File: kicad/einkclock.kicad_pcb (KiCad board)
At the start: 2 copper layers, 80 x 50 mm, 78 parts, among them P1 SWD, Q1 BSH205, Q2 BSH205, Q3 IRLML6244, Q4 IRLML6244, U1 23LC512, U10 DCF77_Generic, U2 LPC1227FBD48/301, U3 TS321ILT, U4 ED060SC4V2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

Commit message: Cleanups
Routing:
- net /E-Ink/-20V: track 101.0 -> 100.2 mm
- net /DCF77/SIG: track 70.0 -> 69.4 mm

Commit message: Cleanups
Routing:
- net /CPU/DON: track 63.5 -> 76.3 mm, vias 3 -> 6
- net Net-(C9-Pad1): track 54.8 -> 66.4 mm
- net GND: track 67.5 -> 74.2 mm, vias 46 -> 45
- net /CPU/DCKV: track 19.9 -> 22.4 mm
- net /CPU/DSPH: track 21.4 -> 19.3 mm
- net /CPU/DOE: track 22.4 -> 20.2 mm
- net /CPU/DCL: track 25.5 -> 23.4 mm
- net /CPU/DSPV: track 13.8 -> 14.6 mm
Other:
- rule trace_min: 0.2 -> 0.25

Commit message: Adjustments
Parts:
- added ?: MountingHole_5mm, Mounting_Holes:MountingHole_5mm, F.Cu at (96.0, 66.0)
- added ?: MountingHole_5mm, Mounting_Holes:MountingHole_5mm, F.Cu at (24.0, 66.0)
- added ?: OSHW-Logo2_7.3x6mm_SilkScreen, Symbols:OSHW-Logo2_7.3x6mm_SilkScreen, F.Cu at (96.0, 23.5)
- moved L3 0.50 mm to (24.0, 39.5)
- moved L6 0.50 mm to (38.5, 39.5)
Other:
- board text added: "+"
- board text added: "-"
- board text added: "E-INK CLOCK REV 1"

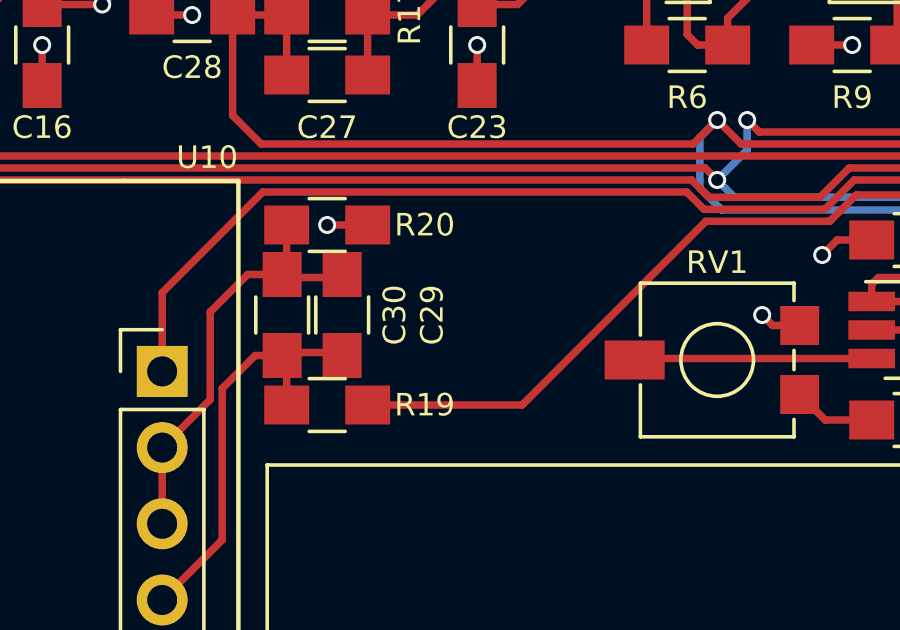
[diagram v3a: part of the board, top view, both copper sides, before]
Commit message: Finish BOM and fix PCB according to the parts
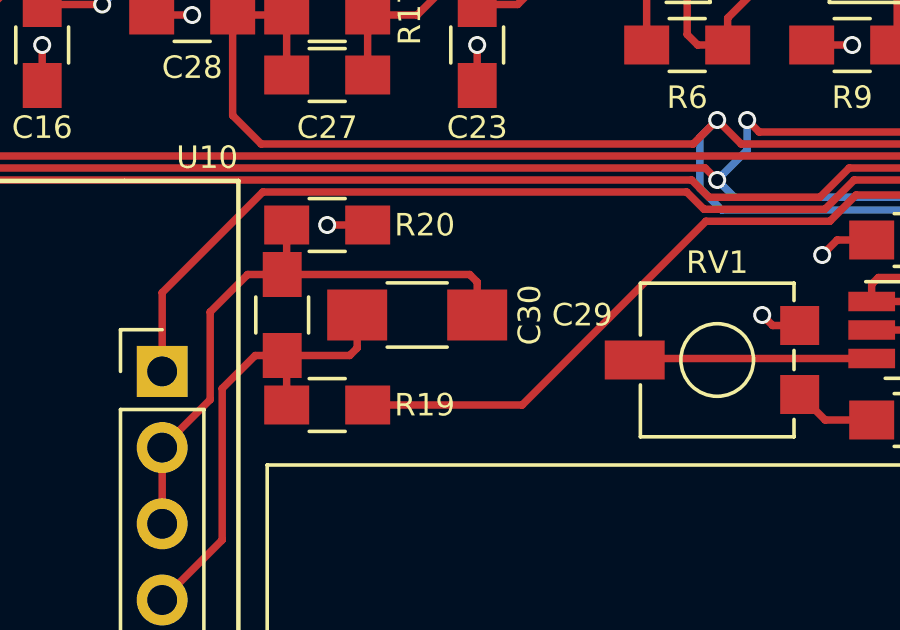
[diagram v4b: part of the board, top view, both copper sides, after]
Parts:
- C29: footprint Resistors_SMD:R_0805_HandSoldering -> Resistors_SMD:R_1206_HandSoldering
- moved C29 2.50 mm to (46.5, 54.0), turned to 180 degrees
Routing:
- net Net-(C29-Pad1): track 14.7 -> 20.5 mm
- net Net-(C29-Pad2): track 14.9 -> 16.2 mm
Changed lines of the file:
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@@
     (thickness 1.6)
     (drawings 11)
-    (tracks 788)
+    (tracks 791)
     (zones 0)
     (modules 81)
@@
     (pcb_text_size 1.5 1.5)
     (mod_edge_width 0.15)
-    (mod_text_size 1 1)
+    (mod_text_size 0.75 0.75)
     (mod_text_width 0.15)
     (pad_size 5 5)
@@
   )
   (module Resistors_SMD:R_0805_HandSoldering (layer F.Cu)
-    (at 44 54 270)
-    (descr "Resistor SMD 0805, hand soldering")
-    (tags "resistor 0805")
-    (attr smd)
-    (fp_text reference C29 (at 0 -3 270) (layer F.SilkS)
-      (effects (font (size 0.75 0.75) (thickness 0.15)))
-    )
-    (fp_text value 100µ (at 0 1.75 270) (layer F.Fab)
-      (effects (font (size 1 1) (thickness 0.15)))
-    )
-    (fp_text user %R (at 0 -1.7 270) (layer F.Fab)
-      (effects (font (size 1 1) (thickness 0.15)))
-    )
-    (fp_line (start -1 0.62) (end -1 -0.62) (layer F.Fab) (width 0.1))
-    (fp_line (start 1 0.62) (end -1 0.62) (layer F.Fab) (width 0.1))
-    (fp_line (start 1 -0.62) (end 1 0.62) (layer F.Fab) (width 0.1))
-    (fp_line (start -1 -0.62) (end 1 -0.62) (layer F.Fab) (width 0.1))
-    (fp_line (start 0.6 0.88) (end -0.6 0.88) (layer F.SilkS) (width 0.12))
-    (fp_line (start -0.6 -0.88) (end 0.6 -0.88) (layer F.SilkS) (width 0.12))
-    (fp_line (start -2.35 -0.9) (end 2.35 -0.9) (layer F.CrtYd) (width 0.05))
-    (fp_line (start -2.35 -0.9) (end -2.35 0.9) (layer F.CrtYd) (width 0.05))
-    (fp_line (start 2.35 0.9) (end 2.35 -0.9) (layer F.CrtYd) (width 0.05))
-    (fp_line (start 2.35 0.9) (end -2.35 0.9) (layer F.CrtYd) (width 0.05))
-    (pad 1 smd rect (at -1.35 0 270) (size 1.5 1.3) (layers F.Cu F.Paste F.Mask)
-      (net 26 "Net-(C29-Pad1)"))
-    (pad 2 smd rect (at 1.35 0 270) (size 1.5 1.3) (layers F.Cu F.Paste F.Mask)
-      (net 27 "Net-(C29-Pad2)"))
-    (model Resistors_SMD.3dshapes/R_0805.wrl
-      (at (xyz 0 0 0))
-      (scale (xyz 1 1 1))
-      (rotate (xyz 0 0 0))
-    )
-  )
-  (module Resistors_SMD:R_0805_HandSoldering (layer F.Cu)
     (at 42 54 270)
     (descr "Resistor SMD 0805, hand soldering")
     (tags "resistor 0805")
     (attr smd)
-    (fp_text reference C30 (at 0 -3.75 270) (layer F.SilkS)
+    (fp_text reference C30 (at 0 -8.25 270) (layer F.SilkS)
       (effects (font (size 0.75 0.75) (thickness 0.15)))
     )
@@
       (net 44 /CPU/DCKV))
   )
-  (module Symbols:OSHW-Logo2_7.3x6mm_SilkScreen (layer F.Cu)
+  (module Symbols:OSHW-Logo2_7.3x6mm_SilkScreen locked (layer F.Cu)
     (at 96 23.5)
     (descr "Open Source Hardware Symbol")
@@
       (xy -0.113933 -2.757629) (xy -0.013056 -2.757714) (xy 0 -2.757714) (xy 0.10391 -2.757652)) (layer F.SilkS) (width 0.01))
   )
+  (module Resistors_SMD:R_1206_HandSoldering (layer F.Cu)
+    (at 46.5 54 180)
+    (descr "Resistor SMD 1206, hand soldering")
+    (tags "resistor 1206")
+    (attr smd)
+    (fp_text reference C29 (at -5.5 0 360) (layer F.SilkS)
+      (effects (font (size 0.75 0.75) (thickness 0.15)))
+    )
+    (fp_text value 100µ (at 0 1.9 180) (layer F.Fab)
+      (effects (font (size 1 1) (thickness 0.15)))
+    )
+    (fp_text user %R (at 0 0 180) (layer F.Fab)
+      (effects (font (size 0.7 0.7) (thickness 0.105)))
+    )
+    (fp_line (start -1.6 0.8) (end -1.6 -0.8) (layer F.Fab) (width 0.1))
+    (fp_line (start 1.6 0.8) (end -1.6 0.8) (layer F.Fab) (width 0.1))
+    (fp_line (start 1.6 -0.8) (end 1.6 0.8) (layer F.Fab) (width 0.1))
+    (fp_line (start -1.6 -0.8) (end 1.6 -0.8) (layer F.Fab) (width 0.1))
+    (fp_line (start 1 1.07) (end -1 1.07) (layer F.SilkS) (width 0.12))
+    (fp_line (start -1 -1.07) (end 1 -1.07) (layer F.SilkS) (width 0.12))
+    (fp_line (start -3.25 -1.11) (end 3.25 -1.11) (layer F.CrtYd) (width 0.05))
+    (fp_line (start -3.25 -1.11) (end -3.25 1.1) (layer F.CrtYd) (width 0.05))
+    (fp_line (start 3.25 1.1) (end 3.25 -1.11) (layer F.CrtYd) (width 0.05))
+    (fp_line (start 3.25 1.1) (end -3.25 1.1) (layer F.CrtYd) (width 0.05))
+    (pad 1 smd rect (at -2 0 180) (size 2 1.7) (layers F.Cu F.Paste F.Mask)
+      (net 26 "Net-(C29-Pad1)"))
+    (pad 2 smd rect (at 2 0 180) (size 2 1.7) (layers F.Cu F.Paste F.Mask)
+      (net 27 "Net-(C29-Pad2)"))
+    (model ${KISYS3DMOD}/Resistors_SMD.3dshapes/R_1206.wrl
+      (at (xyz 0 0 0))
+      (scale (xyz 1 1 1))
+      (rotate (xyz 0 0 0))
+    )
+  )
   (gr_text "E-INK CLOCK\nREV 1" (at 68 23.5) (layer F.SilkS)
     (effects (font (size 1.5 1.5) (thickness 0.3)))
@@
   (segment (start 47.15 41.95) (end 44.9 41.95) (width 0.25) (layer F.Cu) (net 25) (status 30))
   (segment (start 44.9 41.95) (end 44.85 42) (width 0.25) (layer F.Cu) (net 25) (status 30))
+  (segment (start 42 52.65) (end 48.25 52.65) (width 0.25) (layer F.Cu) (net 26))
+  (segment (start 48.25 52.65) (end 48.5 52.9) (width 0.25) (layer F.Cu) (net 26))
+  (segment (start 48.5 52.9) (end 48.5 54) (width 0.25) (layer F.Cu) (net 26))
   (segment (start 39.59999 53.90001) (end 40.85 52.65) (width 0.25) (layer F.Cu) (net 26))
   (segment (start 40.85 52.65) (end 42 52.65) (width 0.25) (layer F.Cu) (net 26) (status 20))
@@
   (segment (start 42.15 51) (end 42.15 52.6) (width 0.25) (layer F.Cu) (net 26) (status 30))
   (segment (start 42.15 52.6) (end 42 52.75) (width 0.25) (layer F.Cu) (net 26) (status 30))
-  (segment (start 42 52.75) (end 44 52.75) (width 0.25) (layer F.Cu) (net 26) (status 30))
   (segment (start 41.79 52.96) (end 42 52.75) (width 0.25) (layer F.Cu) (net 26) (status 30))
+  (segment (start 42 55.35) (end 44.25 55.35) (width 0.25) (layer F.Cu) (net 27))
+  (segment (start 44.25 55.35) (end 44.5 55.1) (width 0.25) (layer F.Cu) (net 27))
+  (segment (start 44.5 55.1) (end 44.5 54) (width 0.25) (layer F.Cu) (net 27))
   (segment (start 40 56.45) (end 40 61.5) (width 0.25) (layer F.Cu) (net 27))
   (segment (start 40 61.5) (end 38 63.5) (width 0.25) (layer F.Cu) (net 27) (status 20))
   (segment (start 42 55.35) (end 41.1 55.35) (width 0.25) (layer F.Cu) (net 27) (status 10))
   (segment (start 41.1 55.35) (end 40 56.45) (width 0.25) (layer F.Cu) (net 27))
-  (segment (start 42 55.25) (end 44 55.25) (width 0.25) (layer F.Cu) (net 27) (status 30))
   (segment (start 41.75 55.5) (end 42 55.25) (width 0.25) (layer F.Cu) (net 27) (status 30))
   (segment (start 42.15 57) (end 42.15 55.4) (width 0.25) (layer F.Cu) (net 27) (status 30))
   (segment (start 42.15 55.4) (end 42 55.25) (width 0.25) (layer F.Cu) (net 27) (status 30))
-  (segment (start 43.75 55.5) (end 44 55.25) (width 0.25) (layer F.Cu) (net 27) (status 30))
   (segment (start 27.15 28.05) (end 26.85 28.05) (width 0.25) (layer F.Cu) (net 28) (status 30))
   (segment (start 26.85 28.05) (end 26.7 27.9) (width 0.25) (layer F.Cu) (net 28) (status 30))
@@
   (segment (start 61.65 57.5) (end 60.1 57.5) (width 0.25) (layer F.Cu) (net 37) (status 10))
   (segment (start 60.1 57.5) (end 59.25 56.65) (width 0.25) (layer F.Cu) (net 37) (status 20))
+  (segment (start 60.256377 50.875021) (end 61.131398 50) (width 0.25) (layer F.Cu) (net 38))
+  (segment (start 56.124979 50.875021) (end 60.256377 50.875021) (width 0.25) (layer F.Cu) (net 38))
+  (segment (start 50 57) (end 56.124979 50.875021) (width 0.25) (layer F.Cu) (net 38))
+  (segment (start 44.85 57) (end 50 57) (width 0.25) (layer F.Cu) (net 38) (status 10))
+  (segment (start 44.85 57) (end 44.95 57) (width 0.25) (layer F.Cu) (net 38) (status 30))
   (segment (start 82.575 38.925) (end 85.575 38.925) (width 0.25) (layer B.Cu) (net 38))
   (segment (start 85.575 38.925) (end 86 38.5) (width 0.25) (layer B.Cu) (net 38))
@@
   (segment (start 78 50.5) (end 77.424999 51.075001) (width 0.25) (layer F.Cu) (net 38))
   (segment (start 75.648998 50) (end 76.723999 51.075001) (width 0.25) (layer F.Cu) (net 38))
-  (segment (start 60.256377 50.875021) (end 61.131398 50) (width 0.25) (layer F.Cu) (net 38))
-  (segment (start 56.124979 50.875021) (end 60.256377 50.875021) (width 0.25) (layer F.Cu) (net 38))
   (segment (start 76.723999 51.075001) (end 77.424999 51.075001) (width 0.25) (layer F.Cu) (net 38))
-  (segment (start 50 57) (end 56.124979 50.875021) (width 0.25) (layer F.Cu) (net 38))
   (segment (start 61.131398 50) (end 75.648998 50) (width 0.25) (layer F.Cu) (net 38))
-  (segment (start 44.85 57) (end 50 57) (width 0.25) (layer F.Cu) (net 38) (status 10))
   (segment (start 83.85 38.25) (end 84.25 38.25) (width 0.25) (layer F.Cu) (net 38) (status 30))
-  (segment (start 44.85 57) (end 44.95 57) (width 0.25) (layer F.Cu) (net 38) (status 30))
   (segment (start 61.65 55.45) (end 53.8 55.45) (width 0.25) (layer F.Cu) (net 39) (status 30))
   (segment (start 53.8 55.45) (end 53.75 55.5) (width 0.25) (layer F.Cu) (net 39) (status 30))
